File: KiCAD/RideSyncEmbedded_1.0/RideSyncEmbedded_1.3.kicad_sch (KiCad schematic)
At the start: 57 parts, among them IC1 LTC3108, IC2 SIP32431DR3-T1GE3, IC3 MAX40018ATA+, IC4 SIP32432DR3-T1GE3, IC5 INA190A4QDCKRQ1, IC6 MAX40018ATA+, IC7 INA190A4QDCKRQ1, J1 Conn_01x02_Pin, J2 Conn_01x02_Pin, T1 LPR6235-752SMRB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

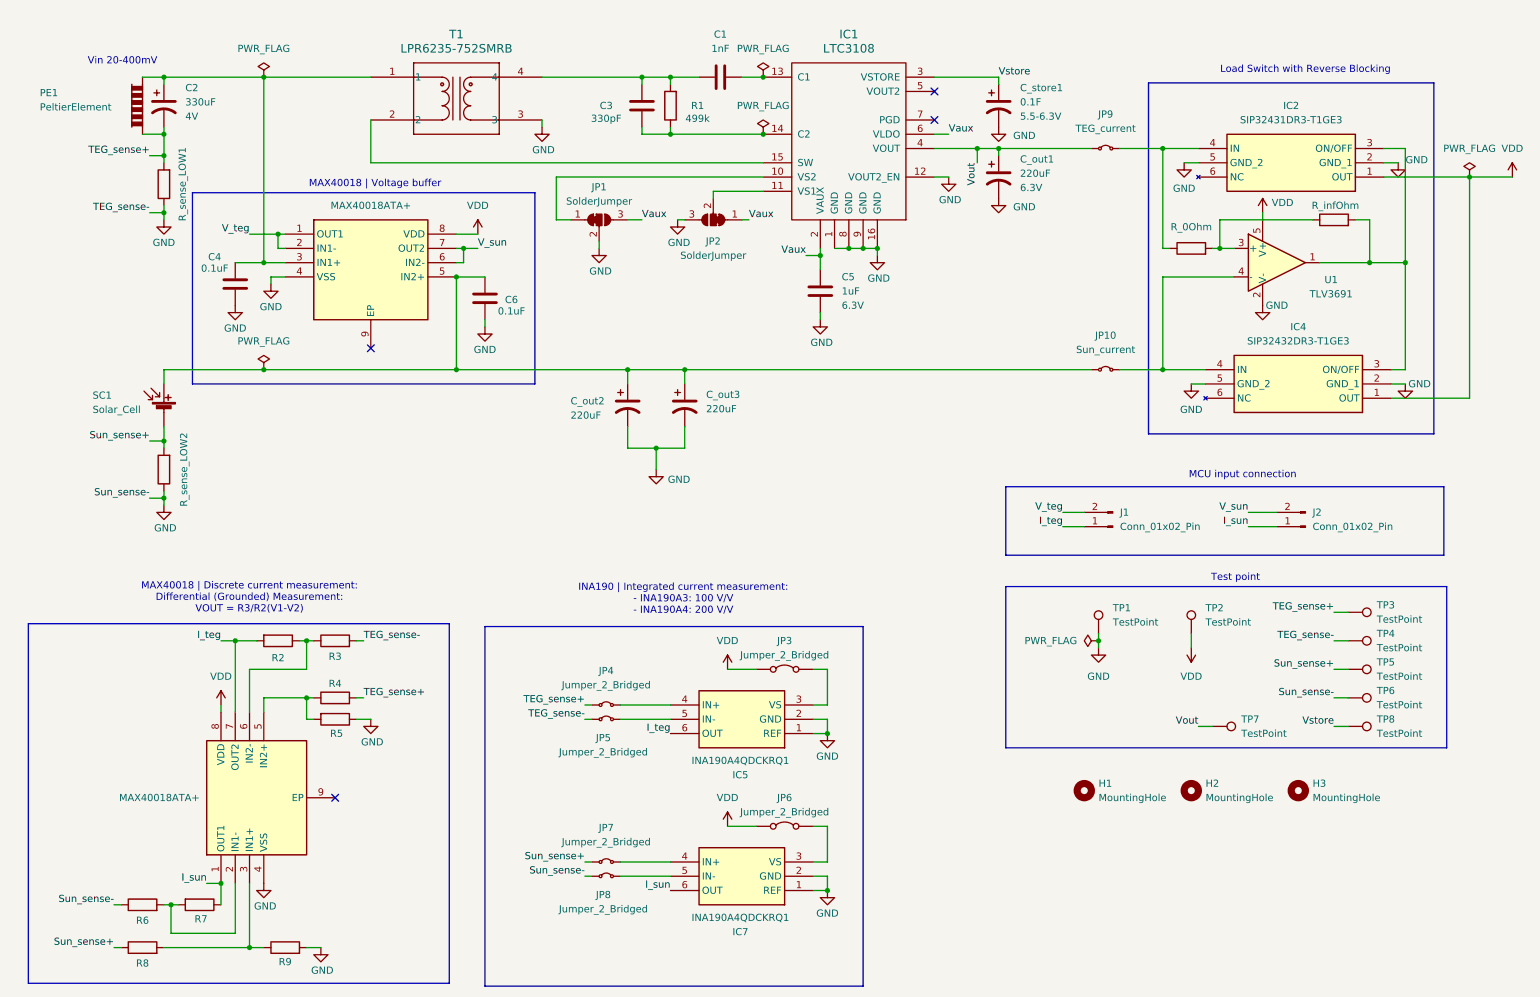
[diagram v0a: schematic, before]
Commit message: load switch config comparison
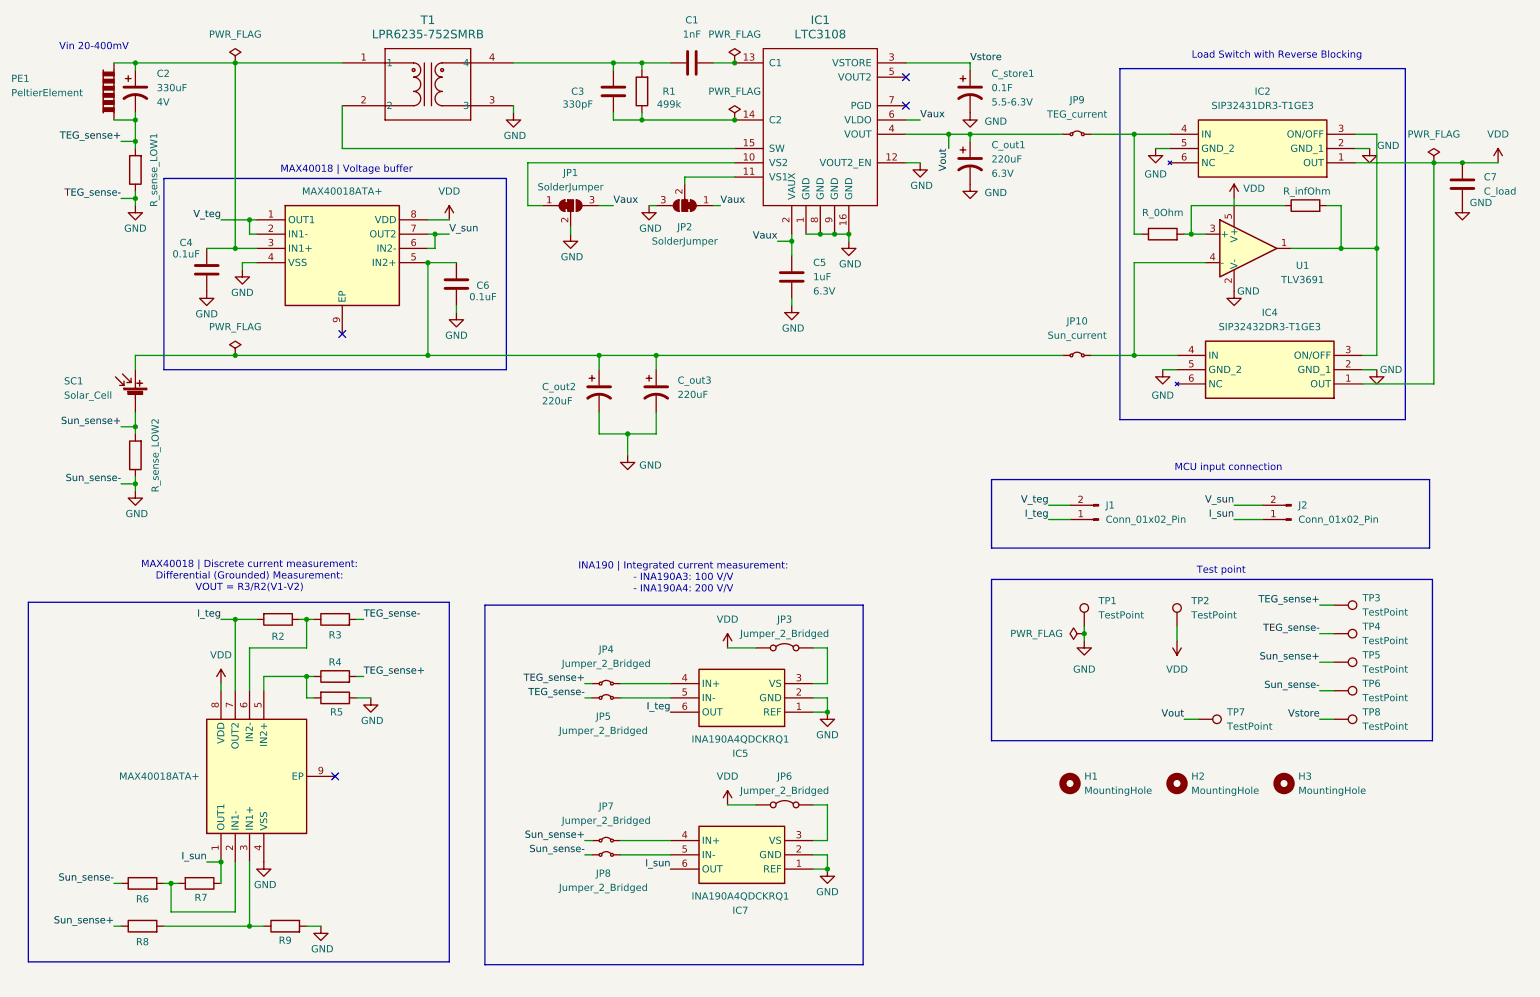
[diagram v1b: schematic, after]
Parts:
- added C7: C_load, symbol Device:C
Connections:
- net GND: now also C7.2
- net VDD: now also C7.1
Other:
- moved on the sheet: C1, C2, C3, C4, C5, C6, C_out1, C_out2, C_out3, C_store1, H1, H2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
